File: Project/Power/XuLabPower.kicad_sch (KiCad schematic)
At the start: 15 parts, among them J1 1986660-2, Q1 PMOS, U1 AP63203WU

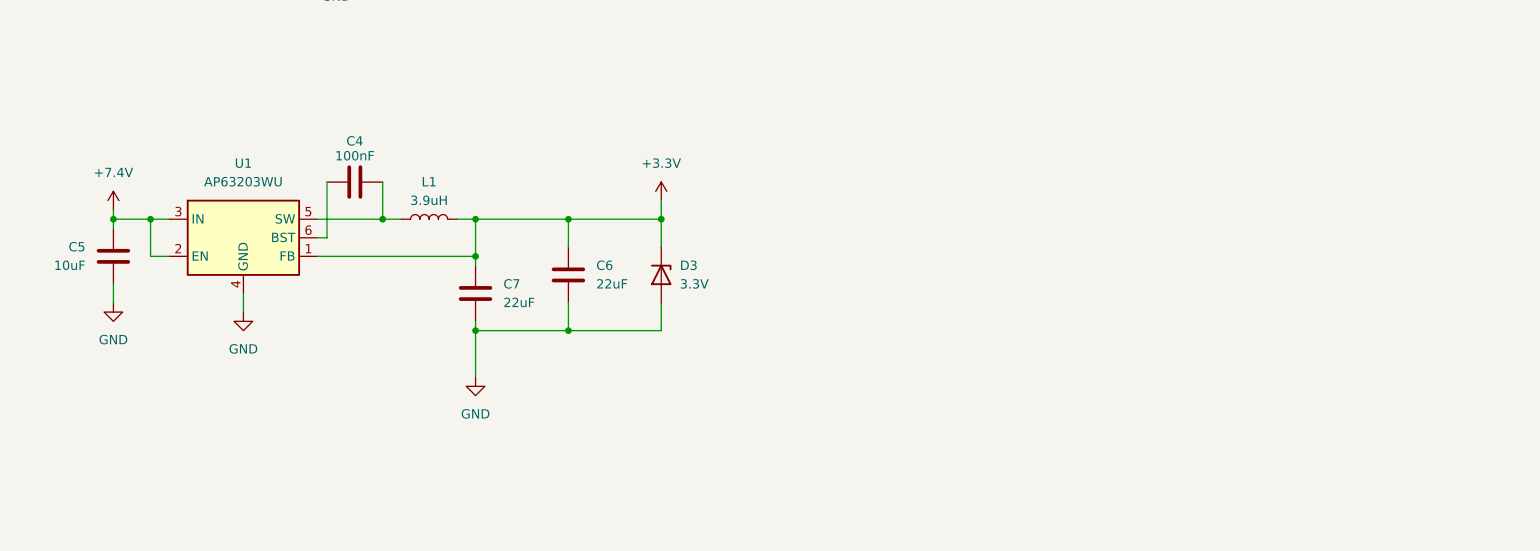
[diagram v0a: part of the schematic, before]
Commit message: Move buck converter to separate sheet
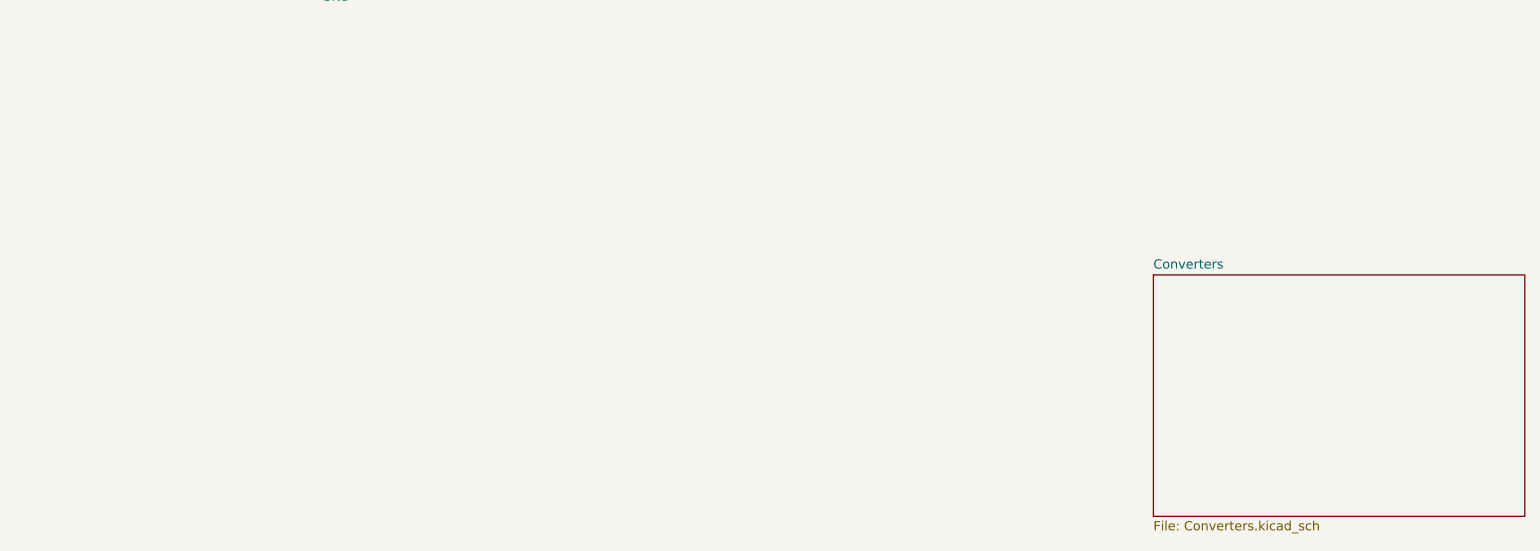
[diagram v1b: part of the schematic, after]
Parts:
- removed C4: 100nF, Capacitor_SMD:C_0402_1005Metric, symbol Device:C
- removed C5: 10uF, Capacitor_SMD:C_1206_3216Metric, symbol Device:C
- removed C6, C7: 22uF, Capacitor_SMD:C_0603_1608Metric, symbol Device:C
- removed D3: 3.3V, Diode_SMD:D_MicroSMP_KA, symbol Device:D_Zener
- removed L1: 3.9uH, Inductor_SMD:L_Pulse_PA4334, symbol Device:L
- removed U1: AP63203WU, Package_TO_SOT_SMD:TSOT-23-6, symbol Regulator_Switching:AP63203WU
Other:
- added sheet Converters (Converters.kicad_sch)

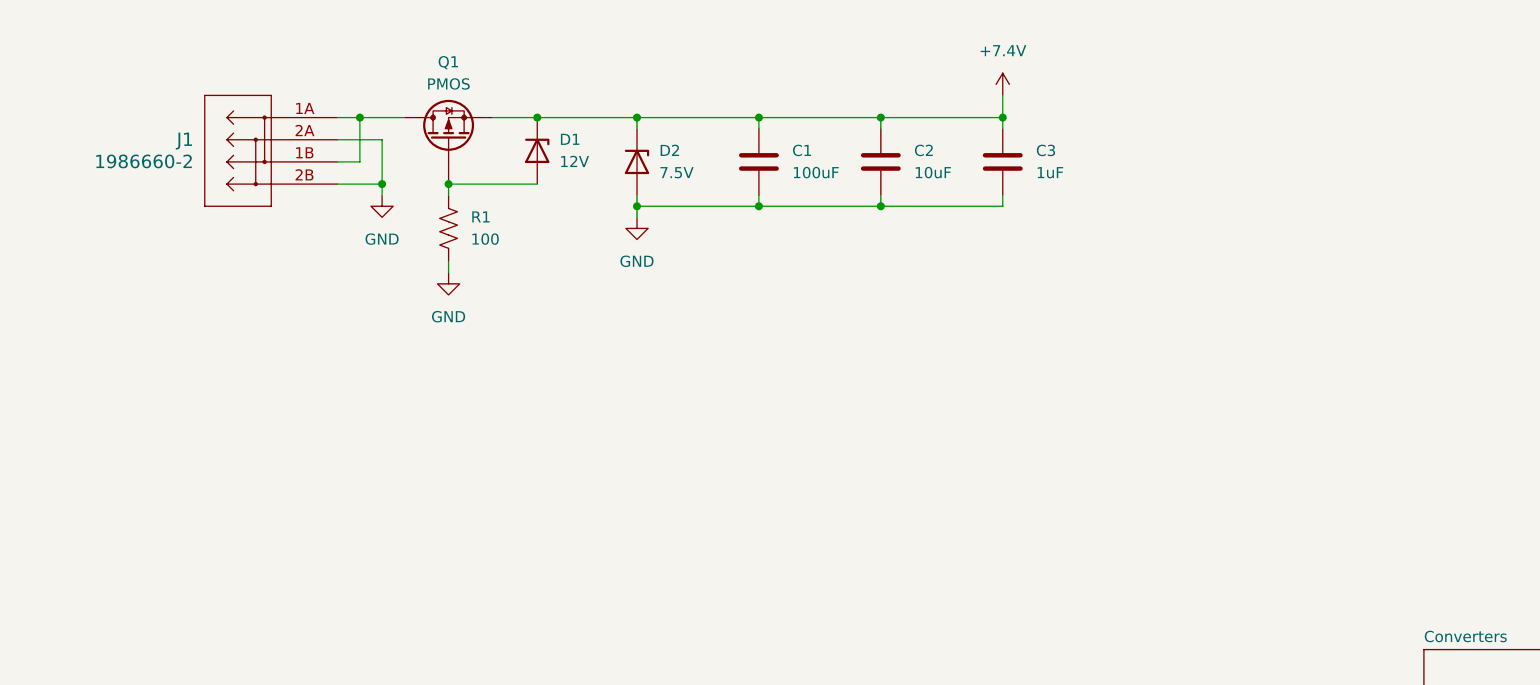
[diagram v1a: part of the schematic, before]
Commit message: Change power connector to XT60
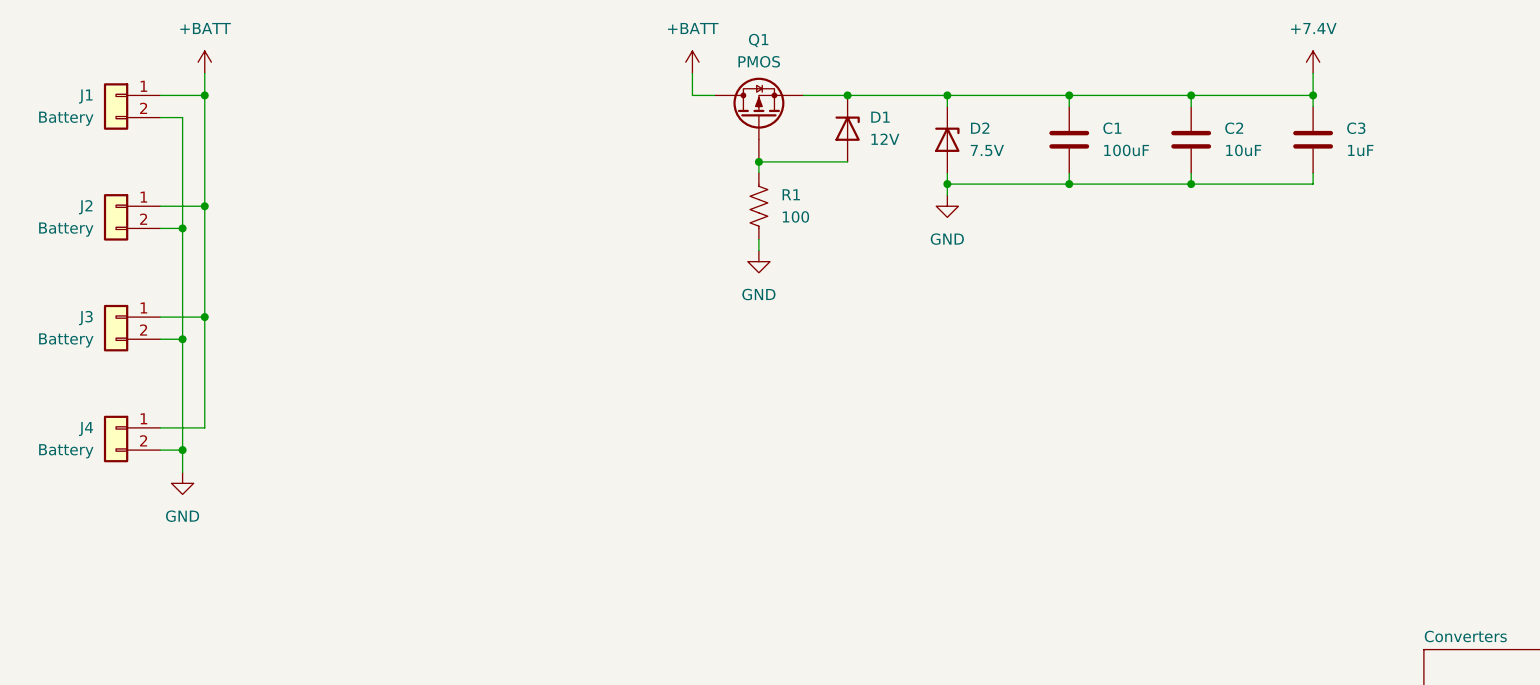
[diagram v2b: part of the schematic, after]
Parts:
- removed J1: 1986660-2, XuLab:CONN2_1986660-2_TEC, symbol XuLab:1986660-2
- added J1, J2, J3, J4: Battery, Connector_AMASS:AMASS_XT60PW-M_1x02_P7.20mm_Horizontal, symbol Connector_Generic:Conn_01x02
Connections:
- net GND: now also J1.2 (Pin_2), J2.2 (Pin_2), J3.2 (Pin_2), J4.2 (Pin_2)
- net +BATT: now reaches Q1.3 (D)
- net +BATT: now also J1.1 (Pin_1), J2.1 (Pin_1), J3.1 (Pin_1), J4.1 (Pin_1)
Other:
- moved on the sheet: C1, C2, C3, D1, D2, Q1, R1

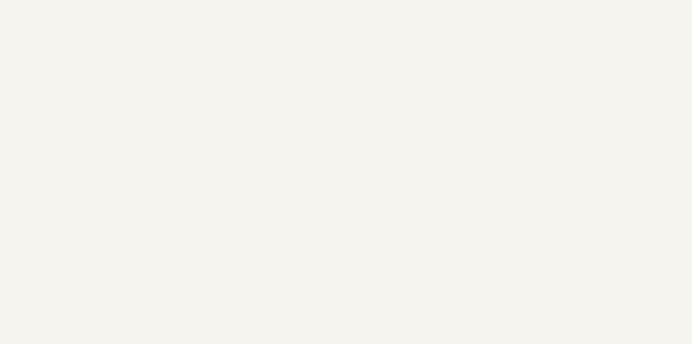
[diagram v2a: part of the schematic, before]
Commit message: Add mounting holes
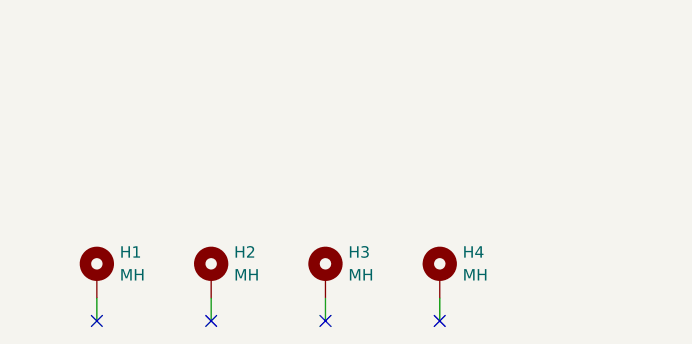
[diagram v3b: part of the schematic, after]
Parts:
- added H1, H2, H3, H4: MH, MountingHole:MountingHole_2.7mm_M2.5_Pad_Via, symbol Mechanical:MountingHole_Pad
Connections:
- no-connect marks 0 -> 4

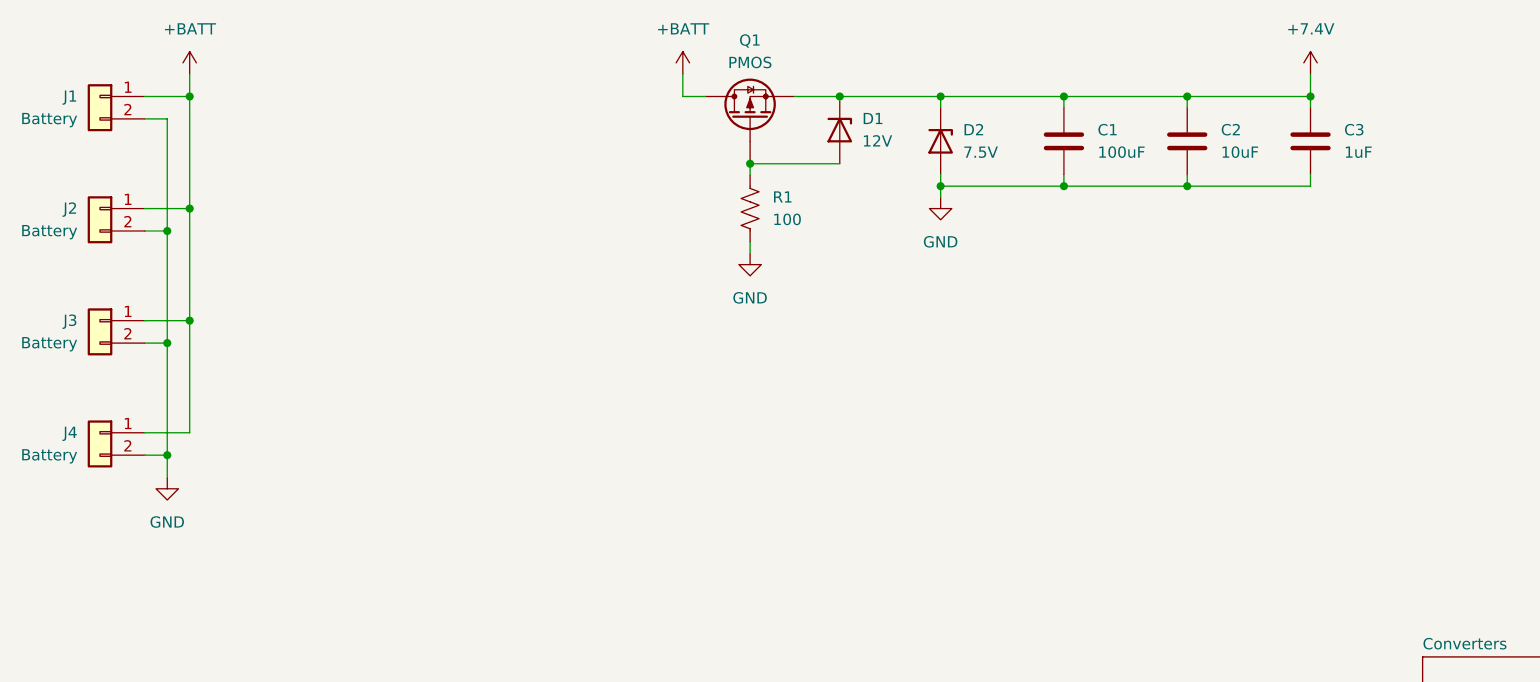
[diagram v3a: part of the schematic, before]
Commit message: Add high-side power switch with LM74502
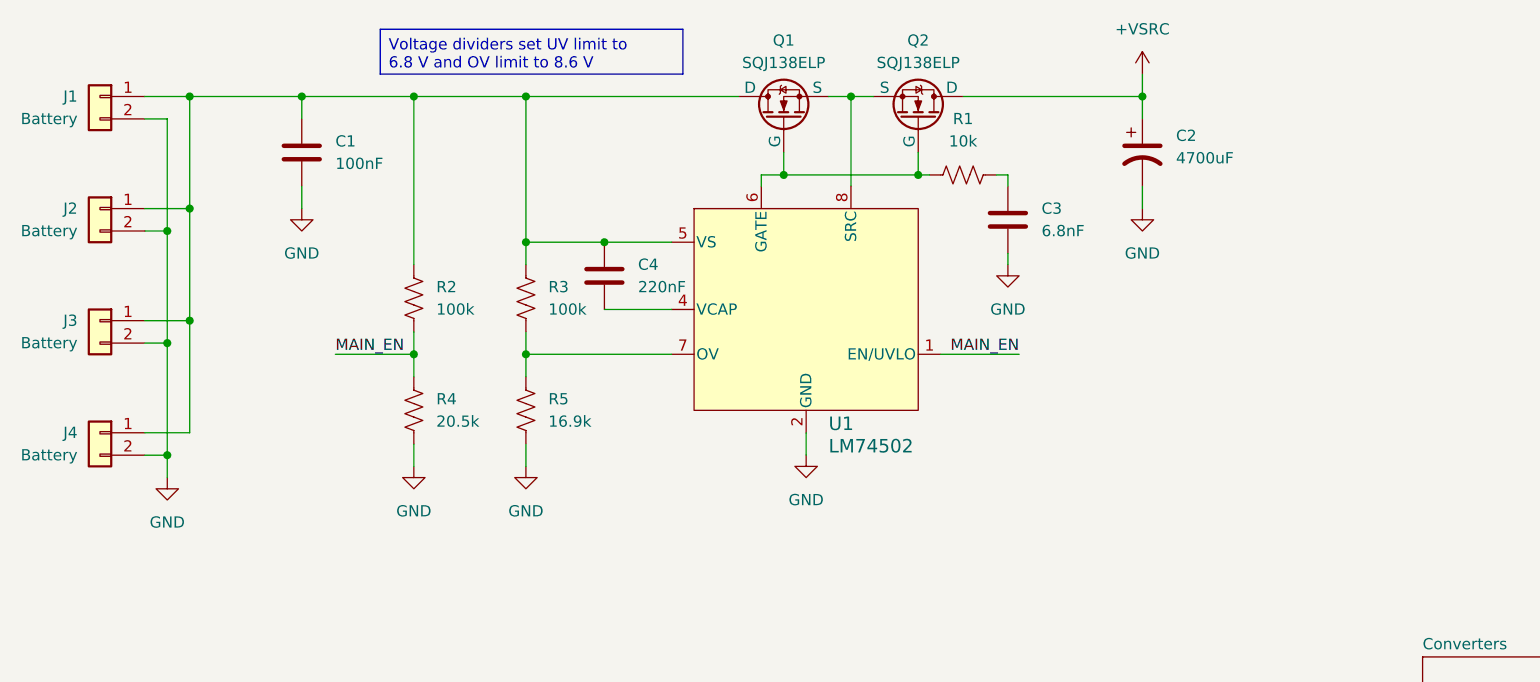
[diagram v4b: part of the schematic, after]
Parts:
- removed C2: 10uF, Capacitor_SMD:C_1206_3216Metric, symbol Device:C
- removed D1: 12V, Diode_SMD:D_SOD-123, symbol Device:D_Zener
- removed D2: 7.5V, Diode_SMD:D_SMB, symbol Device:D_Zener
- removed Q1: PMOS, XuLab:SOP-Advance-8, symbol Device:Q_PMOS
- added C2: 4700uF, Capacitor_THT:CP_Radial_D12.5mm_P5.00mm, symbol Device:C_Polarized_US
- added C4: 220nF, Capacitor_SMD:C_0603_1608Metric, symbol Device:C
- added Q1, Q2: SQJ138ELP, XuLab:PowerPAK_SO-8L, symbol Simulation_SPICE:NMOS
- added R2, R3: 100k, Resistor_SMD:R_0603_1608Metric, symbol Device:R_US
- added R4: 20.5k, Resistor_SMD:R_0603_1608Metric, symbol Device:R_US
- added R5: 16.9k, Resistor_SMD:R_0603_1608Metric, symbol Device:R_US
- added U1: LM74502, Package_TO_SOT_SMD:TSOT-23-8, symbol XuLab:LM74502
- C1: value 100uF -> 100nF; footprint Capacitor_SMD:C_1210_3225Metric -> Capacitor_SMD:C_0603_1608Metric; Listing https://www.digikey.com/en/products/detail/samsung-electro-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 -> https://www.digikey.com/en/products/detail/yageo/CC0603KRX7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
- C3: value 1uF -> 6.8nF; Listing https://www.digikey.com/en/products/detail/samsung-electro-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 -> https://www.digikey.com/en/products/detail/murata-electroni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
- J1, J2, J3, J4: Interchangeable (none) -> No
- R1: value 100 -> 10k; footprint Resistor_SMD:R_1206_3216Metric -> Resistor_SMD:R_0603_1608Metric; Listing https://www.digikey.com/en/products/detail/koa-speer-electr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 -> https://www.digikey.com/en/products/detail/yageo/RC0603FR-0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
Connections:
- net +BATT is gone; now on an unnamed net: J1.1 (Pin_1), J2.1 (Pin_1), J3.1 (Pin_1), J4.1 (Pin_1)
- net GND: now also C2.2, R4.2, R5.2, U1.2 (GND); no longer R1.2
- net at R1.1: now also Q1.4 (G), Q2.4 (G), U1.6 (GATE)
- net +7.4V: no longer names the net of C1.1
- net +7.4V: now also C4.1, Q1.5 (D), R2.1, R3.1, U1.5 (VS); no longer C3.1
- new net: Q1.1 (S), Q1.2 (S), Q1.3 (S), Q2.1 (S), Q2.2 (S), Q2.3 (S), U1.8 (SRC)
- new net: C3.1, R1.2
- new net: R3.2, R5.1, U1.7 (OV)
- new net: C4.2, U1.4 (VCAP)
- new net +VSRC: C2.1, Q2.5 (D)
- new net MAIN_EN: R2.2, R4.1, U1.1 (EN/UVLO)

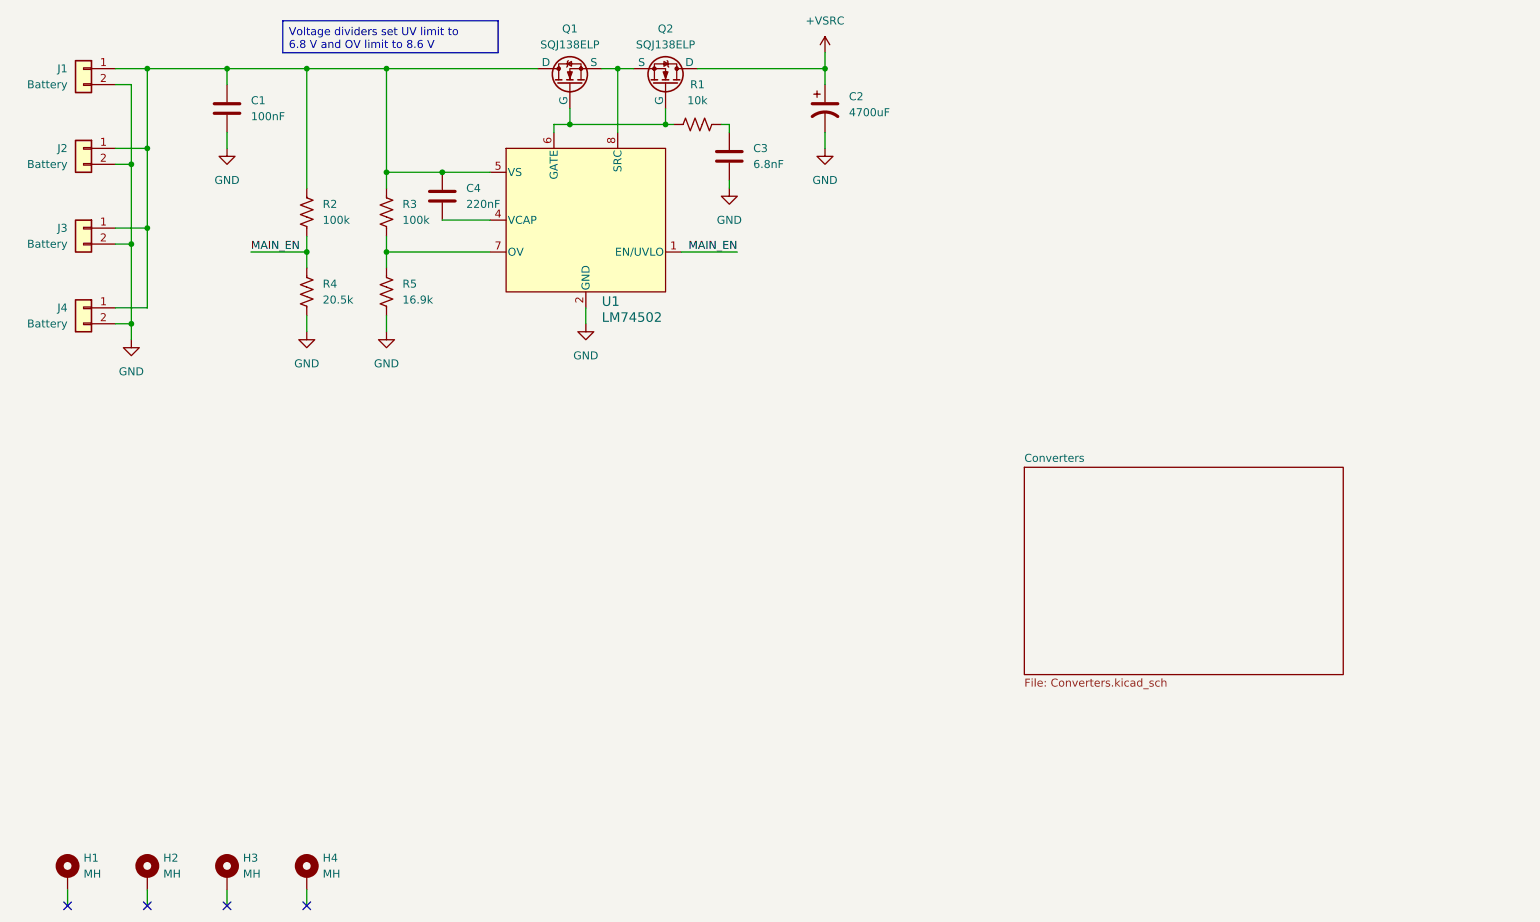
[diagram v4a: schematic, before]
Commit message: Add ideal diode to battery inputs using NCV68061
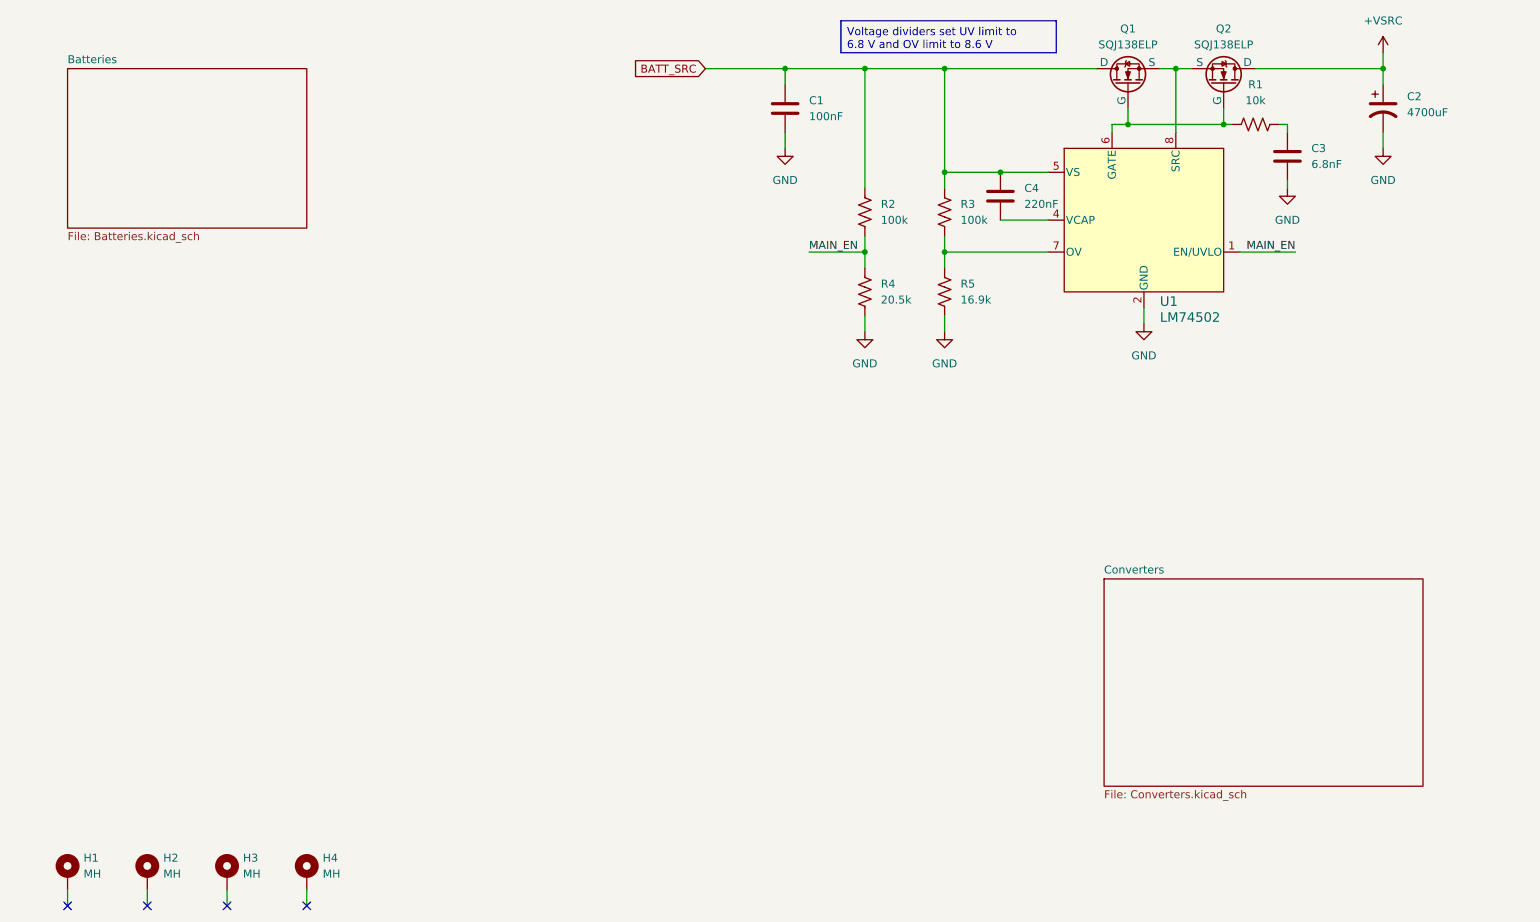
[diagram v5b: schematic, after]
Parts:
- removed J1, J2, J3, J4: Battery, Connector_AMASS:AMASS_XT60PW-M_1x02_P7.20mm_Horizontal, symbol Connector_Generic:Conn_01x02
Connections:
- net BATT_SRC: now reaches C1.1, C4.1, Q1.5 (D), R2.1, R3.1, U1.5 (VS)
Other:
- added sheet Batteries (Batteries.kicad_sch)
- moved on the sheet: C1, C2, C3, C4, Q1, Q2, R1, R2, R3, R4, R5, U1
